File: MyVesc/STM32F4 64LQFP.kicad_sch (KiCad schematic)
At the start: 16 parts, among them J5 UNUSED MCU PINS, P5 SWD, U5 STM32F405RGT6, Y1 8M

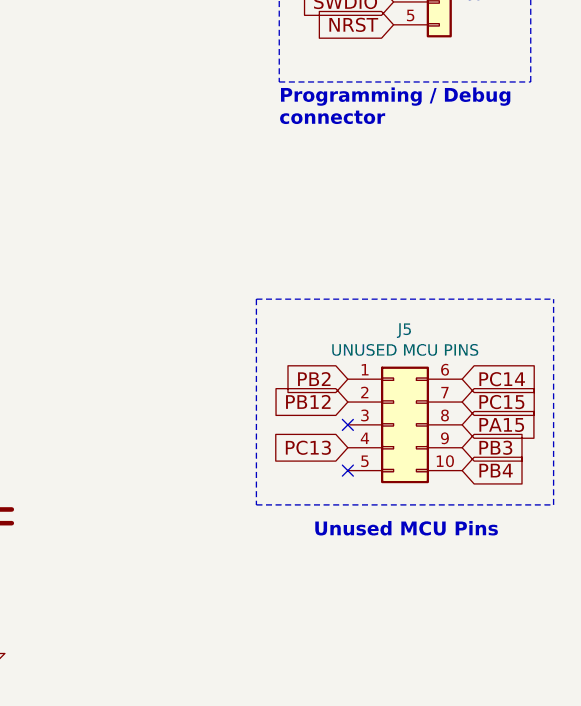
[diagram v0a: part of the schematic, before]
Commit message: routerd logic board
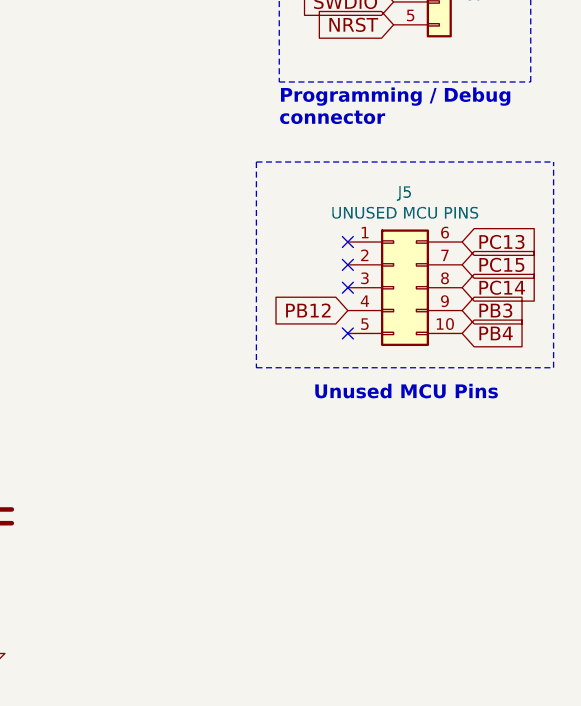
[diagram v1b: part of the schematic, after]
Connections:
- net PA15: no longer J5.8 (Pin_8)
- net PB12: now also J5.4 (Pin_4); no longer J5.2 (Pin_2)
- net PB2: no longer J5.1 (Pin_1)
- net PC13: now also J5.6 (Pin_6); no longer J5.4 (Pin_4)
- net PC14: now also J5.8 (Pin_8); no longer J5.6 (Pin_6)
- no-connect marks 2 -> 4
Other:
- moved on the sheet: J5
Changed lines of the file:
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@@
 	)
 	(no_connect
-		(at 243.84 133.35)
+		(at 243.84 107.95)
 	)
 	(no_connect
-		(at 243.84 128.27)
+		(at 243.84 118.11)
+	)
+	(no_connect
+		(at 243.84 110.49)
+	)
+	(no_connect
+		(at 243.84 113.03)
 	)
 	(wire
@@
 	(polyline
 		(pts
-			(xy 233.68 137.16) (xy 266.7 137.16)
+			(xy 233.68 121.92) (xy 266.7 121.92)
 		)
 		(stroke
@@
 	(polyline
 		(pts
-			(xy 233.68 114.3) (xy 233.68 137.16)
+			(xy 233.68 99.06) (xy 233.68 121.92)
 		)
 		(stroke
@@
 	(polyline
 		(pts
-			(xy 233.68 114.3) (xy 266.7 114.3)
+			(xy 233.68 99.06) (xy 266.7 99.06)
 		)
 		(stroke
@@
 	(polyline
 		(pts
-			(xy 266.7 137.16) (xy 266.7 114.3)
+			(xy 266.7 121.92) (xy 266.7 99.06)
 		)
 		(stroke
@@
 	(text "Unused MCU Pins\n"
 		(exclude_from_sim no)
-		(at 240.03 140.97 0)
+		(at 240.03 125.73 0)
 		(effects
 			(font
@@
 	(global_label "PB3"
 		(shape input)
-		(at 256.54 130.81 0)
+		(at 256.54 115.57 0)
 		(effects
 			(font
@@
 		)
 		(property "Intersheetrefs" "${INTERSHEET_REFS}"
-			(at 256.54 130.81 0)
+			(at 256.54 115.57 0)
 			(effects
 				(font
@@
 		)
 	)
-	(global_label "SWCLK"
+	(global_label "PC13"
 		(shape input)
-		(at 248.92 76.2 180)
+		(at 256.54 107.95 0)
 		(effects
 			(font
 				(size 1.524 1.524)
 			)
-			(justify right)
+			(justify left)
 		)
 		(property "Intersheetrefs" "${INTERSHEET_REFS}"
-			(at 248.92 76.2 0)
+			(at 256.54 107.95 0)
 			(effects
 				(font
@@
 		)
 	)
-	(global_label "PA15"
+	(global_label "SWCLK"
 		(shape input)
-		(at 189.23 81.28 0)
+		(at 248.92 76.2 180)
 		(effects
 			(font
 				(size 1.524 1.524)
 			)
-			(justify left)
+			(justify right)
 		)
 		(property "Intersheetrefs" "${INTERSHEET_REFS}"
-			(at 189.23 81.28 0)
+			(at 248.92 76.2 0)
 			(effects
 				(font
@@
 		)
 	)
-	(global_label "PB3"
+	(global_label "PA15"
 		(shape input)
-		(at 179.07 83.82 0)
+		(at 189.23 81.28 0)
 		(effects
 			(font
@@
 		)
 		(property "Intersheetrefs" "${INTERSHEET_REFS}"
-			(at 179.07 83.82 0)
+			(at 189.23 81.28 0)
 			(effects
 				(font
@@
 		)
 	)
-	(global_label "PC14"
+	(global_label "PB3"
 		(shape input)
-		(at 256.54 123.19 0)
+		(at 179.07 83.82 0)
 		(effects
 			(font
@@
 		)
 		(property "Intersheetrefs" "${INTERSHEET_REFS}"
-			(at 256.54 123.19 0)
+			(at 179.07 83.82 0)
 			(effects
 				(font
@@
 	(global_label "PB4"
 		(shape input)
-		(at 256.54 133.35 0)
+		(at 256.54 118.11 0)
 		(effects
 			(font
@@
 		)
 		(property "Intersheetrefs" "${INTERSHEET_REFS}"
-			(at 256.54 133.35 0)
+			(at 256.54 118.11 0)
 			(effects
 				(font
@@
 		)
 	)
-	(global_label "SWDIO"
+	(global_label "PC14"
 		(shape input)
-		(at 179.07 76.2 0)
+		(at 256.54 113.03 0)
 		(effects
 			(font
@@
 		)
 		(property "Intersheetrefs" "${INTERSHEET_REFS}"
-			(at 179.07 76.2 0)
+			(at 256.54 113.03 0)
 			(effects
 				(font
@@
 		)
 	)
-	(global_label "PA15"
+	(global_label "PB12"
 		(shape input)
-		(at 256.54 128.27 0)
+		(at 243.84 115.57 180)
 		(effects
 			(font
 				(size 1.524 1.524)
 			)
-			(justify left)
+			(justify right)
 		)
 		(property "Intersheetrefs" "${INTERSHEET_REFS}"
-			(at 256.54 128.27 0)
+			(at 243.84 115.57 0)
 			(effects
 				(font
@@
 		)
 	)
-	(global_label "PB2"
+	(global_label "SWDIO"
 		(shape input)
-		(at 243.84 123.19 180)
+		(at 179.07 76.2 0)
 		(effects
 			(font
 				(size 1.524 1.524)
 			)
-			(justify right)
+			(justify left)
 		)
 		(property "Intersheetrefs" "${INTERSHEET_REFS}"
-			(at 243.84 123.19 0)
+			(at 179.07 76.2 0)
 			(effects
 				(font
@@
 	(global_label "PC15"
 		(shape input)
-		(at 256.54 125.73 0)
+		(at 256.54 110.49 0)
 		(effects
 			(font
@@
 		)
 		(property "Intersheetrefs" "${INTERSHEET_REFS}"
-			(at 256.54 125.73 0)
+			(at 256.54 110.49 0)
 			(effects
 				(font
@@
 		)
 	)
-	(global_label "PC13"
-		(shape input)
-		(at 243.84 130.81 180)
-		(effects
-			(font
-				(size 1.524 1.524)
-			)
-			(justify right)
-		)
-		(property "Intersheetrefs" "${INTERSHEET_REFS}"
-			(at 243.84 130.81 0)
-			(effects
-				(font
-					(size 1.27 1.27)
-				)
-				(hide yes)
-			)
-		)
-	)
 	(global_label "NRST"
 		(shape input)
@@
 		)
 	)
-	(global_label "PB12"
-		(shape input)
-		(at 243.84 125.73 180)
-		(effects
-			(font
-				(size 1.524 1.524)
-			)
-			(justify right)
-		)
-		(property "Intersheetrefs" "${INTERSHEET_REFS}"
-			(at 243.84 125.73 0)
-			(effects
-				(font
-					(size 1.27 1.27)
-				)
-				(hide yes)
-			)
-		)
-	)
 	(global_label "SWCLK"
 		(shape input)
@@
 	(symbol
 		(lib_id "Connector_Generic:Conn_02x05_Top_Bottom")
-		(at 248.92 128.27 0)
+		(at 248.92 113.03 0)
 		(unit 1)
 		(exclude_from_sim no)
@@
 		(dnp no)
 		(property "Reference" "J5"
-			(at 250.19 117.6782 0)
+			(at 250.19 102.4382 0)
 			(effects
 				(font
@@
 		)
 		(property "Value" "UNUSED MCU PINS"
-			(at 250.19 119.9896 0)
+			(at 250.19 104.7496 0)
 			(effects
 				(font
@@
 		)
 		(property "Footprint" "Connector_PinHeader_2.00mm:PinHeader_2x05_P2.00mm_Vertical"
-			(at 248.92 128.27 0)
+			(at 248.92 113.03 0)
 			(effects
 				(font
@@
 		)
 		(property "Datasheet" "~"
-			(at 248.92 128.27 0)
+			(at 248.92 113.03 0)
 			(effects
 				(font
@@
 		)
 		(property "Description" ""
-			(at 248.92 128.27 0)
+			(at 248.92 113.03 0)
 			(effects
 				(font
